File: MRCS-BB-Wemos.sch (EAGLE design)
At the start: 11 parts, among them IC1 MCP23017SP

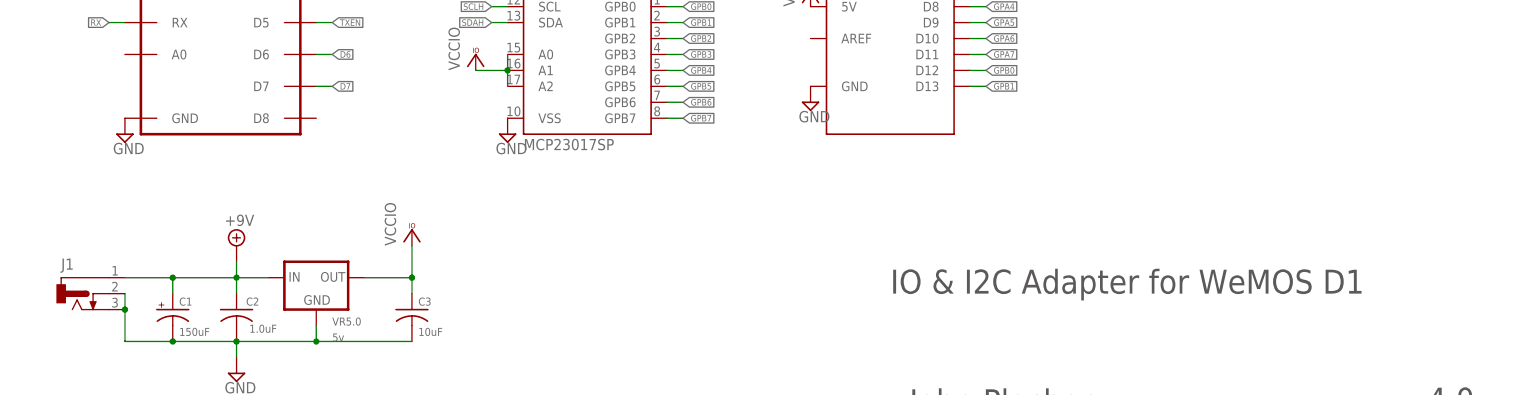
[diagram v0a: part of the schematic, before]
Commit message: replace / update components with newer ones in SPCoast library clean up silk screen, add MRCS
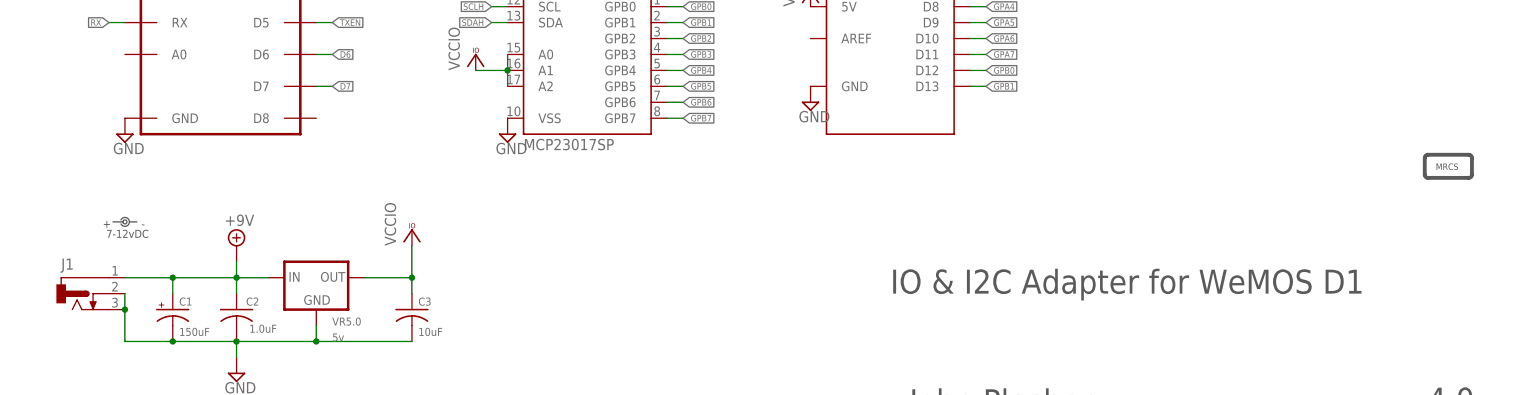
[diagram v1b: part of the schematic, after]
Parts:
- added U$1: DOC-MRCS-LOGOTOP, SPCoast:DOC-MRCS-LOGOTOP
- IC1: device microchip:MCP23017SP -> SPCoast:MCP23017SP
- LABEL1: device SPCoast-minimal:POWER_LABEL -> SPCoast:DOC-POWER_LABEL
- OSHW1: value OSHW-LOGOL -> DOC-OSHW-LOGO-L; device SparkFun:OSHW-LOGOL -> SPCoast:DOC-OSHW-LOGO-L
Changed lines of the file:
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@@
 <layer number="255" name="routoute" color="7" fill="1" visible="yes" active="yes"/>
 </layers>
-<schematic xreflabel="%F%N/%S.%C%R" xrefpart="/%S.%C%R">
+<schematic xreflabel="%F%N/%S" xrefpart="/%S.%C%R">
 <attributes>
 </attributes>
@@
 <parts>
 <part name="FRAME1" library="MCP" deviceset="FRAME-LETTER" device=""/>
-<part name="OSHW1" library="SparkFun" deviceset="OSHW-LOGO" device="L" value="OSHW-LOGOL"/>
+<part name="OSHW1" library="SPCoast" deviceset="DOC-OSHW-LOGO-" device="L" value="DOC-OSHW-LOGO-L"/>
 <part name="SUPPLY2" library="supply2" deviceset="+9V" device=""/>
 <part name="V12" library="supply2" deviceset="GND" device=""/>
 <part name="J1" library="SPCoast" deviceset="CONNECTOR-DC-POWER" device="-RA"/>
-<part name="LABEL1" library="SPCoast-minimal" deviceset="POWER_LABEL" device="" value="7-12vDC"/>
+<part name="LABEL1" library="SPCoast" deviceset="DOC-POWER_LABEL" device="" value="7-12vDC"/>
 <part name="C3" library="SPCoast" deviceset="CAP*" device="PTH1" value="10uF"/>
 <part name="C2" library="SPCoast" deviceset="CAP*" device="PTH1" value="1.0uF"/>
@@
 <part name="VCC8" library="supply1" deviceset="VCCIO" device=""/>
 <part name="C1" library="SPCoast" deviceset="CAP-POL*" device="PTH-5MM" value="150uF"/>
-<part name="IC1" library="microchip" deviceset="MCP23017" device="SP"/>
+<part name="IC1" library="SPCoast" deviceset="MCP23017" device="SP"/>
 <part name="BBLEO" library="SPCoast" deviceset="ARDUINO-BBLEO" device=""/>
 <part name="V1" library="supply2" deviceset="GND" device=""/>
@@
 <part name="V4" library="supply2" deviceset="GND" device=""/>
 <part name="LS2" library="SPCoast" deviceset="I2C-LEVELSHIFTER" device=""/>
+<part name="U$1" library="SPCoast" deviceset="DOC-MRCS-LOGO" device="TOP"/>
 </parts>
 <sheets>
@@
 <instance part="FRAME1" gate="G$1" x="0" y="0"/>
 <instance part="FRAME1" gate="G$2" x="147.32" y="0"/>
-<instance part="OSHW1" gate="G$1" x="233.68" y="177.8"/>
+<instance part="OSHW1" gate="DOC-OSHW-LOGO" x="233.68" y="177.8"/>
 <instance part="SUPPLY2" gate="G$1" x="45.72" y="33.02" smashed="yes">
 <attribute name="VALUE" x="43.815" y="36.195" size="1.778" layer="96"/>
@@
 <attribute name="VALUE" x="17.78" y="19.05" size="1.778" layer="96"/>
 </instance>
-<instance part="LABEL1" gate="POWERLABEL" x="27.94" y="35.56"/>
+<instance part="LABEL1" gate="PWR1" x="27.94" y="35.56"/>
 <instance part="C3" gate="C1" x="73.66" y="22.86" smashed="yes">
 <attribute name="NAME" x="74.676" y="23.495" size="1.27" layer="95"/>
@@
 <instance part="V4" gate="GND" x="101.6" y="129.54"/>
 <instance part="LS2" gate="LS1" x="104.14" y="147.32"/>
+<instance part="U$1" gate="G$1" x="238.76" y="45.72"/>
 </instances>
 <busses>

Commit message: replace VR with RA version & mounting hole to W/A an eagle bug Add MRCS to sch
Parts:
- VR5.0: device SPCoast:VREG-PTH-FLAT-5 -> SPCoast:VREG-PTH-RA-
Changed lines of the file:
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@@
 <part name="C3" library="SPCoast" deviceset="CAP*" device="PTH1" value="10uF"/>
 <part name="C2" library="SPCoast" deviceset="CAP*" device="PTH1" value="1.0uF"/>
-<part name="VR5.0" library="SPCoast" deviceset="VREG-?-*" device="PTH-FLAT" technology="5" value="5v"/>
+<part name="VR5.0" library="SPCoast" deviceset="VREG-?-*" device="PTH-RA" value="5v"/>
 <part name="WEMOS" library="SPCoast" deviceset="WEMOS-D1" device="V1" value="D1Mini"/>
 <part name="V7" library="supply2" deviceset="GND" device=""/>
